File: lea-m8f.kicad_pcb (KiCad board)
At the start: 2 copper layers, 0 parts

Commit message: Create lib and add footprint for LEA-M8F
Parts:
- added U2: LEA-M8F, LEA, F.Cu at (148.5, 105.0)
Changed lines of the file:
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@@
 (kicad_pcb (version 4) (host pcbnew "(2014-jul-16 BZR unknown)-product")
   (general
-    (links 0)
-    (no_connects 0)
+    (links 4)
+    (no_connects 4)
     (area 0 0 0 0)
     (thickness 1.6)
@@
     (tracks 0)
     (zones 0)
-    (modules 0)
-    (nets 1)
+    (modules 1)
+    (nets 23)
   )
   (page A4)
@@
   )
   (net 0 "")
+  (net 1 /SDA)
+  (net 2 /SCL)
+  (net 3 /TXD)
+  (net 4 /RXD)
+  (net 5 "Net-(U2-Pad5)")
+  (net 6 VCC)
+  (net 7 GND)
+  (net 8 "Net-(U2-Pad8)")
+  (net 9 "Net-(U2-Pad9)")
+  (net 10 "Net-(U2-Pad10)")
+  (net 11 /VBCKP)
+  (net 12 /SB_N)
+  (net 13 "Net-(U2-Pad16)")
+  (net 14 "Net-(U2-Pad20)")
+  (net 15 "Net-(U2-Pad21)")
+  (net 16 "Net-(U2-Pad22)")
+  (net 17 "Net-(U2-Pad23)")
+  (net 18 /VDDUSB)
+  (net 19 "Net-(CON1-Pad2)")
+  (net 20 "Net-(CON1-Pad3)")
+  (net 21 "Net-(U2-Pad27)")
+  (net 22 /M8F_PPS)
   (net_class Default "This is the default net class."
     (clearance 0.254)
@@
     (uvia_dia 0.508)
     (uvia_drill 0.127)
+    (add_net /M8F_PPS)
+    (add_net /RXD)
+    (add_net /SB_N)
+    (add_net /SCL)
+    (add_net /SDA)
+    (add_net /TXD)
+    (add_net /VBCKP)
+    (add_net /VDDUSB)
+    (add_net GND)
+    (add_net "Net-(CON1-Pad2)")
+    (add_net "Net-(CON1-Pad3)")
+    (add_net "Net-(U2-Pad10)")
+    (add_net "Net-(U2-Pad16)")
+    (add_net "Net-(U2-Pad20)")
+    (add_net "Net-(U2-Pad21)")
+    (add_net "Net-(U2-Pad22)")
+    (add_net "Net-(U2-Pad23)")
+    (add_net "Net-(U2-Pad27)")
+    (add_net "Net-(U2-Pad5)")
+    (add_net "Net-(U2-Pad8)")
+    (add_net "Net-(U2-Pad9)")
+    (add_net VCC)
+  )
+  (module LEA (layer F.Cu)
+    (at 148.5011 105.0036)
+    (tags "u-blox LEA")
+    (fp_text reference U2 (at 0 -12.5) (layer F.SilkS)
+      (effects (font (size 1.5 1.5) (thickness 0.15)))
+    )
+    (fp_text value LEA-M8F (at 0 13.75) (layer F.SilkS)
+      (effects (font (size 1.5 1.5) (thickness 0.15)))
+    )
+    (fp_line (start -8.5 -8.75) (end -8.5 -11.25) (layer F.SilkS) (width 0.15))
+    (fp_line (start -8.5 -11.25) (end 8.25 -11.25) (layer F.SilkS) (width 0.15))
+    (fp_line (start 8.25 -11.25) (end 8.25 -8.75) (layer F.SilkS) (width 0.15))
+    (fp_line (start -8.5 10.25) (end -8.5 12.5) (layer F.SilkS) (width 0.15))
+    (fp_line (start -8.5 12.5) (end 8.25 12.5) (layer F.SilkS) (width 0.15))
+    (fp_line (start 8.25 12.5) (end 8.25 10.25) (layer F.SilkS) (width 0.15))
+    (pad 1 smd rect (at 8.2 9.3) (size 1.8 0.8) (layers F.Cu F.Paste F.Mask)
+      (net 1 /SDA))
+    (pad 2 smd rect (at 8.2 8.2) (size 1.8 0.8) (layers F.Cu F.Paste F.Mask)
+      (net 2 /SCL))
+    (pad 3 smd rect (at 8.2 7.1) (size 1.8 0.8) (layers F.Cu F.Paste F.Mask)
+      (net 3 /TXD))
+    (pad 4 smd rect (at 8.2 6) (size 1.8 0.8) (layers F.Cu F.Paste F.Mask)
+      (net 4 /RXD))
+    (pad 5 smd rect (at 8.2 4.9) (size 1.8 0.8) (layers F.Cu F.Paste F.Mask)
+      (net 5 "Net-(U2-Pad5)"))
+    (pad 6 smd rect (at 8.2 3.8) (size 1.8 0.8) (layers F.Cu F.Paste F.Mask)
+      (net 6 VCC))
+    (pad 7 smd rect (at 8.2 2.7) (size 1.8 0.8) (layers F.Cu F.Paste F.Mask)
+      (net 7 GND))
+    (pad 8 smd rect (at 8.2 1.6) (size 1.8 0.8) (layers F.Cu F.Paste F.Mask)
+      (net 8 "Net-(U2-Pad8)"))
+    (pad 9 smd rect (at 8.2 -2.2) (size 1.8 0.8) (layers F.Cu F.Paste F.Mask)
+      (net 9 "Net-(U2-Pad9)"))
+    (pad 10 smd rect (at 8.2 -3.3) (size 1.8 0.8) (layers F.Cu F.Paste F.Mask)
+      (net 10 "Net-(U2-Pad10)"))
+    (pad 11 smd rect (at 8.2 -4.4) (size 1.8 0.8) (layers F.Cu F.Paste F.Mask)
+      (net 11 /VBCKP))
+    (pad 12 smd rect (at 8.2 -5.5) (size 1.8 0.8) (layers F.Cu F.Paste F.Mask)
+      (net 12 /SB_N))
+    (pad 13 smd rect (at 8.2 -6.6) (size 1.8 0.8) (layers F.Cu F.Paste F.Mask)
+      (net 7 GND))
+    (pad 14 smd rect (at 8.2 -7.7) (size 1.8 0.8) (layers F.Cu F.Paste F.Mask)
+      (net 7 GND))
+    (pad 15 smd rect (at -8.6 -7.7) (size 1.8 0.8) (layers F.Cu F.Paste F.Mask)
+      (net 7 GND))
+    (pad 16 smd rect (at -8.6 -6.6) (size 1.8 0.8) (layers F.Cu F.Paste F.Mask)
+      (net 13 "Net-(U2-Pad16)"))
+    (pad 17 smd rect (at -8.6 -5.5) (size 1.8 0.8) (layers F.Cu F.Paste F.Mask)
+      (net 13 "Net-(U2-Pad16)"))
+    (pad 18 smd rect (at -8.6 -4.4) (size 1.8 0.8) (layers F.Cu F.Paste F.Mask))
+    (pad 19 smd rect (at -8.6 -3.3) (size 1.8 0.8) (layers F.Cu F.Paste F.Mask))
+    (pad 20 smd rect (at -8.6 -2.2) (size 1.8 0.8) (layers F.Cu F.Paste F.Mask)
+      (net 14 "Net-(U2-Pad20)"))
+    (pad 21 smd rect (at -8.6 1.6) (size 1.8 0.8) (layers F.Cu F.Paste F.Mask)
+      (net 15 "Net-(U2-Pad21)"))
+    (pad 22 smd rect (at -8.6 2.7) (size 1.8 0.8) (layers F.Cu F.Paste F.Mask)
+      (net 16 "Net-(U2-Pad22)"))
+    (pad 23 smd rect (at -8.6 3.8) (size 1.8 0.8) (layers F.Cu F.Paste F.Mask)
+      (net 17 "Net-(U2-Pad23)"))
+    (pad 24 smd rect (at -8.6 4.9) (size 1.8 0.8) (layers F.Cu F.Paste F.Mask)
+      (net 18 /VDDUSB))
+    (pad 25 smd rect (at -8.6 6) (size 1.8 0.8) (layers F.Cu F.Paste F.Mask)
+      (net 19 "Net-(CON1-Pad2)"))
+    (pad 26 smd rect (at -8.6 7.1) (size 1.8 0.8) (layers F.Cu F.Paste F.Mask)
+      (net 20 "Net-(CON1-Pad3)"))
+    (pad 27 smd rect (at -8.6 8.2) (size 1.8 0.8) (layers F.Cu F.Paste F.Mask)
+      (net 21 "Net-(U2-Pad27)"))
+    (pad 28 smd rect (at -8.6 9.3) (size 1.8 0.8) (layers F.Cu F.Paste F.Mask)
+      (net 22 /M8F_PPS))
   )
 )

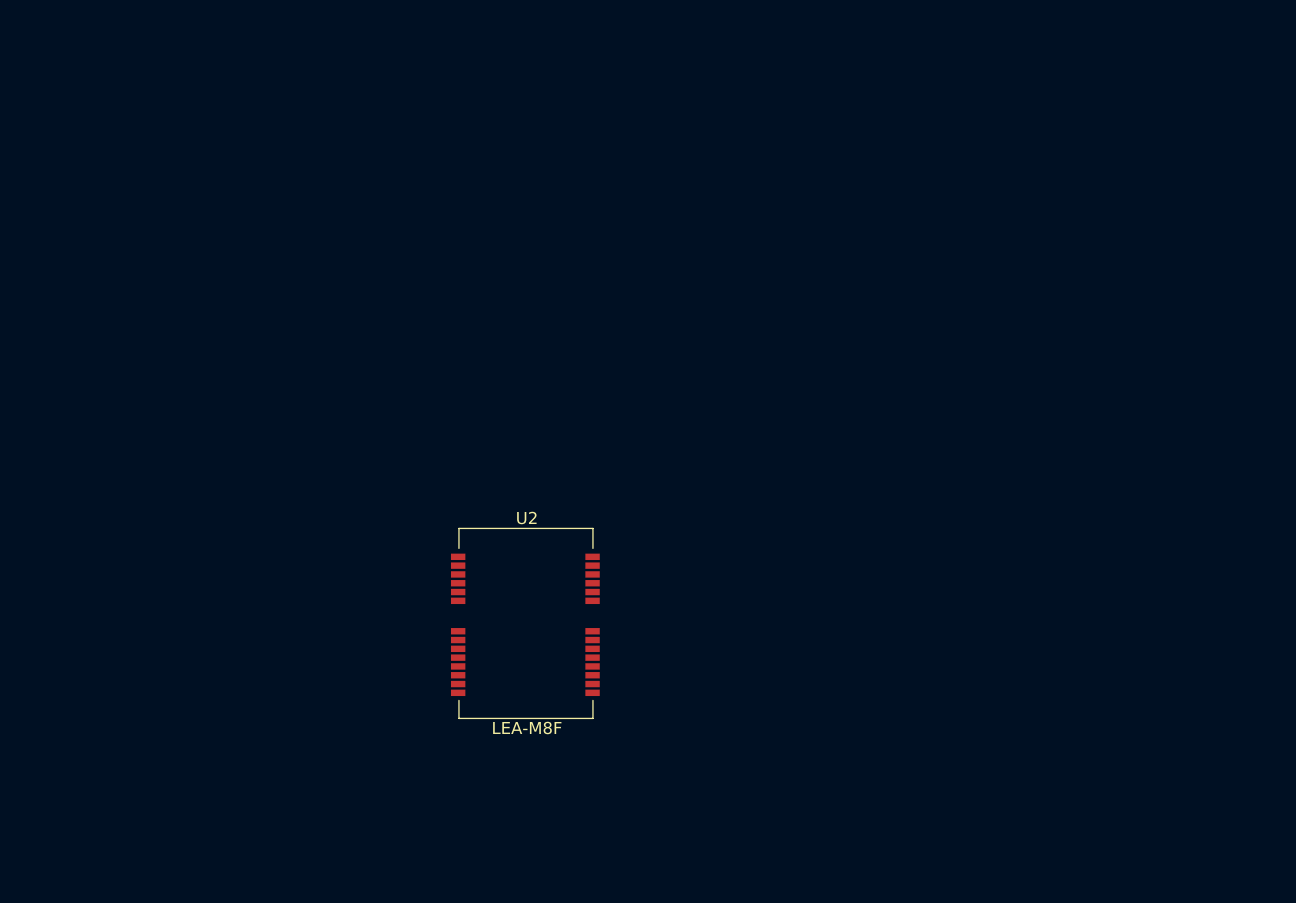
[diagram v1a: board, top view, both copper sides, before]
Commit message: Add components to board
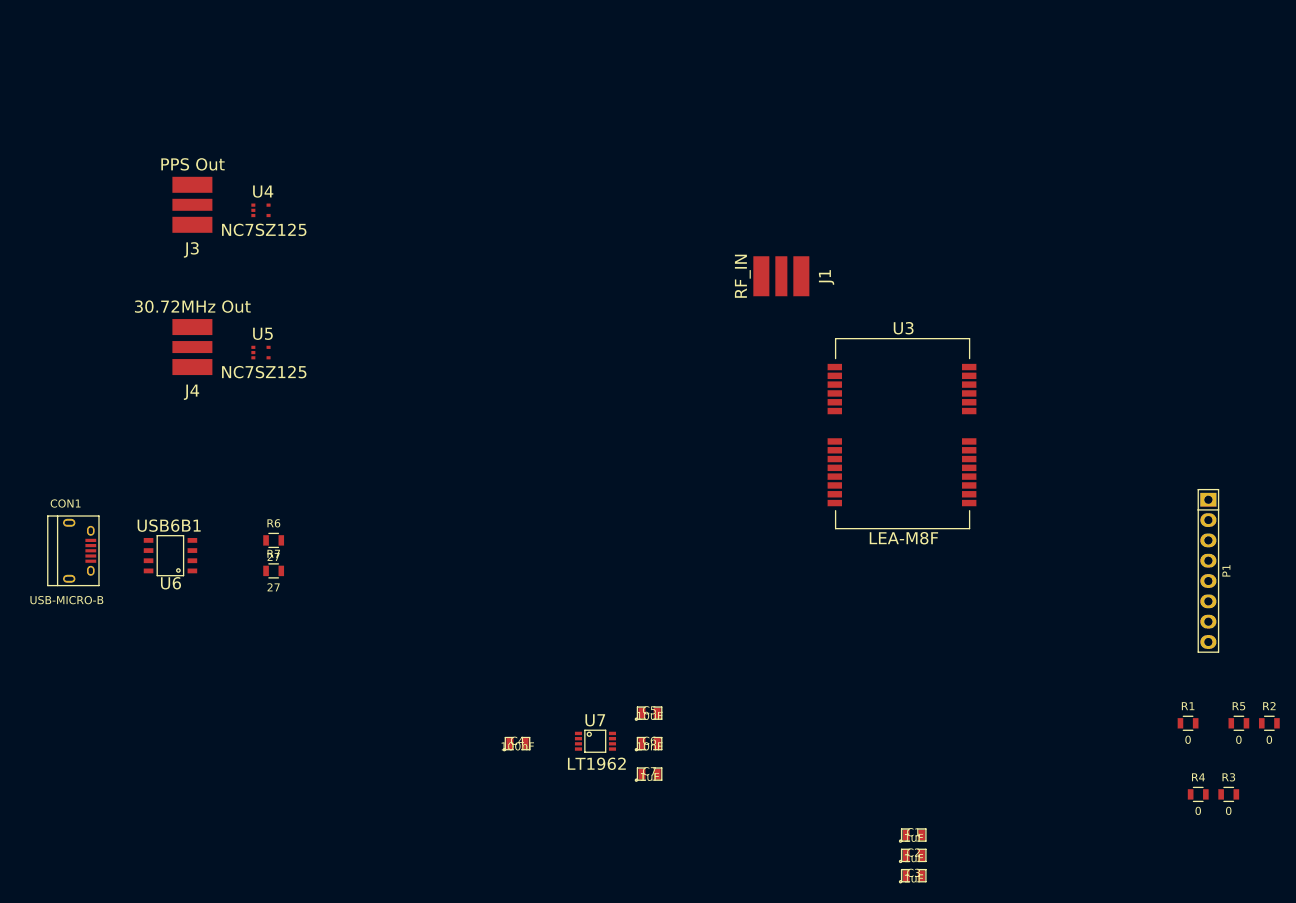
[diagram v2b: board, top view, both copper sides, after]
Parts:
- removed U2: LEA-M8F, LEA
- added C1: 1uF, SMD_Packages:SMD-0805, F.Cu at (196.8, 132.1)
- added C2: 1uF, SMD_Packages:SMD-0805, F.Cu at (196.8, 134.6)
- added C3: 1uF, SMD_Packages:SMD-0805, F.Cu at (196.8, 137.2)
- added C4: 100nF, SMD_Packages:SMD-0805, F.Cu at (147.3, 120.7)
- added C5: 10uF, SMD_Packages:SMD-0805, F.Cu at (163.8, 116.8)
- added C6: 10nF, SMD_Packages:SMD-0805, F.Cu at (163.8, 120.7)
- added C7: 1uF, SMD_Packages:SMD-0805, F.Cu at (163.8, 124.5)
- added CON1: USB-MICRO-B, Connect:USB_Micro-B, F.Cu at (94.0, 95.2)
- added J1: RF_IN, lea-m8f:SMA_SIDE, F.Cu at (177.8, 62.2)
- added J3: PPS Out, lea-m8f:SMA_SIDE, F.Cu at (106.7, 50.8)
- added J4: 30.72MHz Out, lea-m8f:SMA_SIDE, F.Cu at (106.7, 68.6)
- added P1: CONN_01X08, Pin_Headers:Pin_Header_Straight_1x08, F.Cu at (233.7, 99.1)
- added R1: 0, Resistors_SMD:R_0805, F.Cu at (231.1, 118.1)
- added R2: 0, Resistors_SMD:R_0805, F.Cu at (241.3, 118.1)
- added R3: 0, Resistors_SMD:R_0805, F.Cu at (236.2, 127.0)
- added R4: 0, Resistors_SMD:R_0805, F.Cu at (232.4, 127.0)
- added R5: 0, Resistors_SMD:R_0805, F.Cu at (237.5, 118.1)
- added R6: 27, Resistors_SMD:R_0805, F.Cu at (116.8, 95.2)
- added R7: 27, Resistors_SMD:R_0805, F.Cu at (116.8, 99.1)
- added U3: LEA-M8F, lea-m8f:LEA, F.Cu at (195.6, 81.3)
- added U4: NC7SZ125, lea-m8f:SC70, F.Cu at (114.3, 53.3)
- added U5: NC7SZ125, lea-m8f:SC70, F.Cu at (114.3, 71.1)
- added U6: USB6B1, lea-m8f:SO-8, F.Cu at (106.7, 99.1)
- added U7: LT1962, lea-m8f:MS8, F.Cu at (154.9, 119.4)

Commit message: Start place and route
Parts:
- added J2: DB9, Connect:DB9FD, F.Cu at (201.9, 35.6)
- added U100: B200_GPSDO, lea-m8f:GPSDO_B200, F.Cu at (196.8, 73.8)
- added U2: MAX232, Housings_SOIC:SOIC-16_3.9x9.9mm_Pitch1.27mm, F.Cu at (195.3, 58.7)
- R1, R2, R5: moved to B.Cu
- moved J3 115.6 mm to (216.5, 87.1)
- moved C4 112.5 mm to (221.0, 35.6)
- moved J4 110.0 mm to (216.6, 73.2)
- moved U5 95.7 mm to (210.0, 74.4)
- moved U4 83.7 mm to (188.1, 92.8), turned to 270 degrees
- moved C2 80.9 mm to (195.3, 53.7), turned to 180 degrees
- moved C3 78.6 mm to (203.1, 58.8), turned to 90 degrees
- moved C1 78.4 mm to (199.0, 53.7), turned to 180 degrees
- moved R3 75.2 mm to (180.6, 76.3)
- moved CON1 75.1 mm to (168.5, 86.5)
- moved U6 71.1 mm to (177.1, 89.4)
- moved R4 67.3 mm to (180.6, 84.0)
- moved R7 66.2 mm to (181.8, 86.4)
- moved R6 65.2 mm to (181.7, 88.6)
- moved R1 58.5 mm to (194.6, 72.4)
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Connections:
- net Net-(J1-Pad2) renamed /RF_IN
- net Net-(R2-Pad1) renamed /LOCK
- net Net-(U3-Pad9) renamed /REFCLK
- C4 pad 2: (no net) -> GND
- R1 pad 1: (no net) -> Net-(R1-Pad1)
- R3 pad 2: (no net) -> Net-(R3-Pad2)
- R4 pad 2: (no net) -> Net-(R4-Pad2)
- U3 pad 17: (no net) -> GND
- U3 pad 18: (no net) -> /VANT
- U3 pad 19: (no net) -> /VANT
- U6 pad 2: Net-(R7-Pad1) -> Net-(R6-Pad1)
- U6 pad 3: Net-(R6-Pad1) -> Net-(R7-Pad1)
- U6 pad 6: Net-(CON1-Pad3) -> Net-(CON1-Pad2)
- U6 pad 7: Net-(CON1-Pad2) -> Net-(CON1-Pad3)
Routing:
- net /RXD: track 0.00 -> 82.7 mm, vias 0 -> 2
- net /SB_N: track 0.00 -> 41.1 mm, vias 0 -> 1
- net /PPS_BUFF: track 0.00 -> 34.2 mm
- net /5VUSB: track 0.00 -> 27.3 mm
- net /TXD: track 0.00 -> 22.0 mm, vias 0 -> 1
- net /SCL: track 0.00 -> 15.7 mm, vias 0 -> 1
- net /SDA: track 0.00 -> 13.8 mm, vias 0 -> 1
- net /REFCLK_BUFF: track 0.00 -> 13.6 mm
- net Net-(R1-Pad1): track 0.00 -> 12.9 mm
- net /LOCK: track 0.00 -> 8.38 mm
- net /REFCLK: track 0.00 -> 7.02 mm
- net Net-(R6-Pad2): track 0.00 -> 6.08 mm
- net /M8F_PPS: track 0.00 -> 5.95 mm
- net Net-(R7-Pad2): track 0.00 -> 5.20 mm
- net VCC: track 0.00 -> 4.96 mm
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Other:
- net class Default: clearance 0.254 -> 0.2; trace_width 0.254 -> 0.3; via_dia 0.889 -> 0.9; via_drill 0.635 -> 0.6
- net class Power added: clearance 0.2, trace_width 0.45, via_dia 1.2, via_drill 1
- net class RF added: clearance 0.2, trace_width 0.45, via_dia 1, via_drill 0.8
- rule trace_clearance: 0.254 -> 0.2

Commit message: More routing
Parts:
- moved C4 77.7 mm to (192.9, 108.0)
- moved J2 76.9 mm to (201.7, 112.4)
- moved C2 54.8 mm to (202.5, 108.1), turned to 0 degrees
- moved C1 54.4 mm to (198.9, 108.1), turned to 0 degrees
- moved C3 45.7 mm to (195.5, 103.8), turned to 270 degrees
- moved U2 44.9 mm to (202.4, 103.1), turned to 90 degrees
- moved CON1 27.6 mm to (180.6, 111.4), turned to 90 degrees
- moved C6 14.2 mm to (178.7, 89.6)
- moved C5 14.2 mm to (178.7, 87.7)
- moved U7 14.2 mm to (179.0, 91.7)
- moved C7 12.9 mm to (175.3, 93.8)
- moved U6 8.97 mm to (185.1, 93.4), turned to 270 degrees
- moved R7 3.75 mm to (182.1, 90.1), turned to 90 degrees
- moved R6 2.98 mm to (184.3, 90.1), turned to 90 degrees
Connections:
- net Net-(R1-Pad1) renamed /ISP_N
- C3 pad 1: Net-(C3-Pad1) -> VCC
- U2 pad 10: /M8F_PPS -> /PPS_BUFF
- U2 pad 16: Net-(C3-Pad1) -> VCC
- U3 pad 24: (no net) -> VCC
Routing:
- net VCC: track 4.96 -> 155.6 mm, vias 0 -> 6
- net /PPS_BUFF: track 34.2 -> 80.1 mm, vias 0 -> 1
- net /TXD: track 22.0 -> 56.4 mm, vias 1 -> 2
- net /RXD: track 82.7 -> 52.7 mm
- net /SB_N: track 41.1 -> 58.3 mm, vias 1 -> 3
- net Net-(J2-Pad3): track 0.00 -> 13.9 mm, vias 0 -> 1
- net /RF_IN: track 0.00 -> 12.8 mm
- net Net-(J2-Pad2): track 0.00 -> 12.2 mm, vias 0 -> 1
- net Net-(J2-Pad1): track 0.00 -> 11.0 mm
- net Net-(CON1-Pad3): track 3.23 -> 13.3 mm
- net Net-(CON1-Pad2): track 3.19 -> 13.0 mm
- net /5VUSB: track 27.3 -> 34.2 mm
- net Net-(C3-Pad2): track 0.00 -> 4.97 mm
- net Net-(R7-Pad2): track 5.20 -> 8.64 mm
- net Net-(C1-Pad2): track 0.00 -> 2.59 mm
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
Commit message: Check what happens with polygon pours
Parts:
- J3: value PPS Out -> PPS
- J4: value 30.72MHz Out -> 30.72
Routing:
- net GND: track 0.00 -> 50.9 mm, vias 0 -> 9
- added copper zone on B.Cu, net GND
- added copper zone on F.Cu, net GND

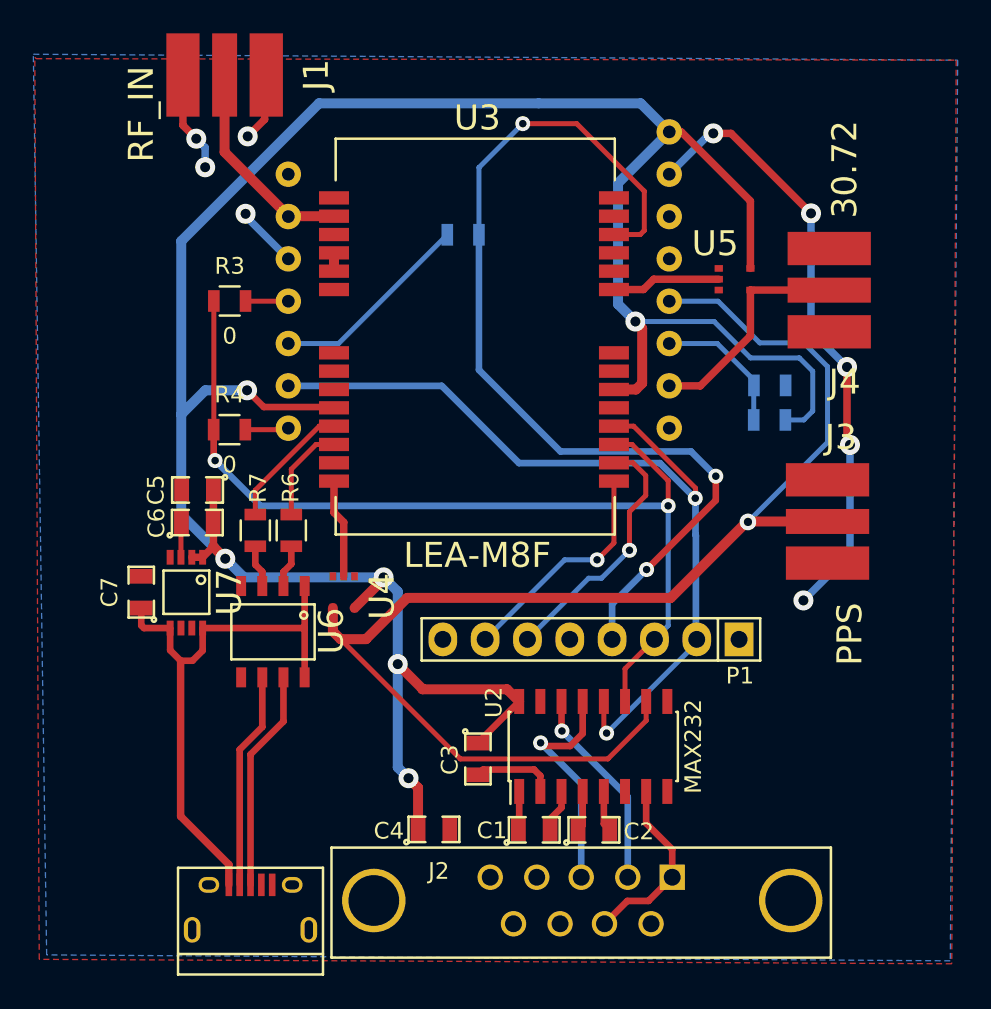
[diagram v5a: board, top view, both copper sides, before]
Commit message: do zone via stitch, correct footprints, revise board outline
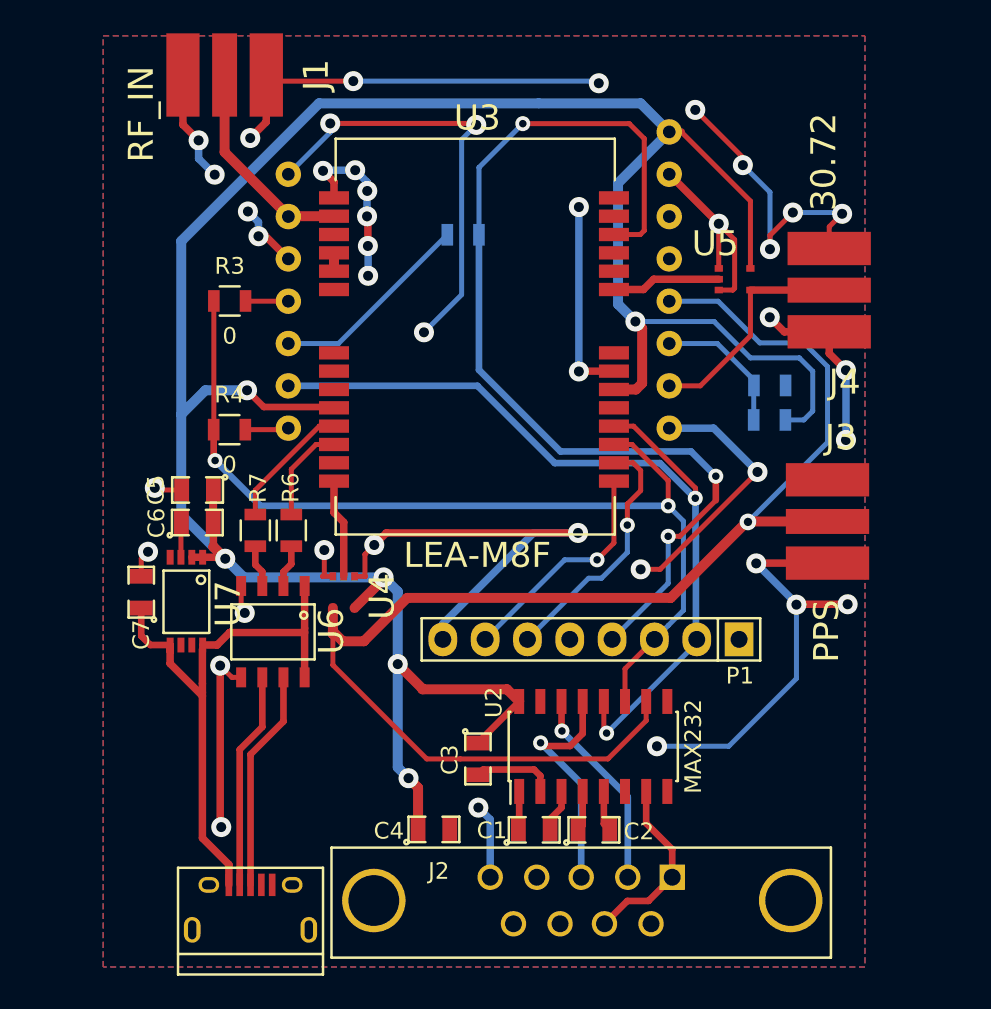
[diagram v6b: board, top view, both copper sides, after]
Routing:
- net GND: track 50.9 -> 216.7 mm, vias 9 -> 42
- net VCC: track 155.6 -> 158.1 mm
- net /PPS_BUFF: track 80.1 -> 82.5 mm
- net /SB_N: track 58.3 -> 60.6 mm
- net /TXD: track 56.4 -> 57.2 mm
- net /5VUSB: track 34.2 -> 34.8 mm
